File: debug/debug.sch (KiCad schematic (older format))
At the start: 6 parts

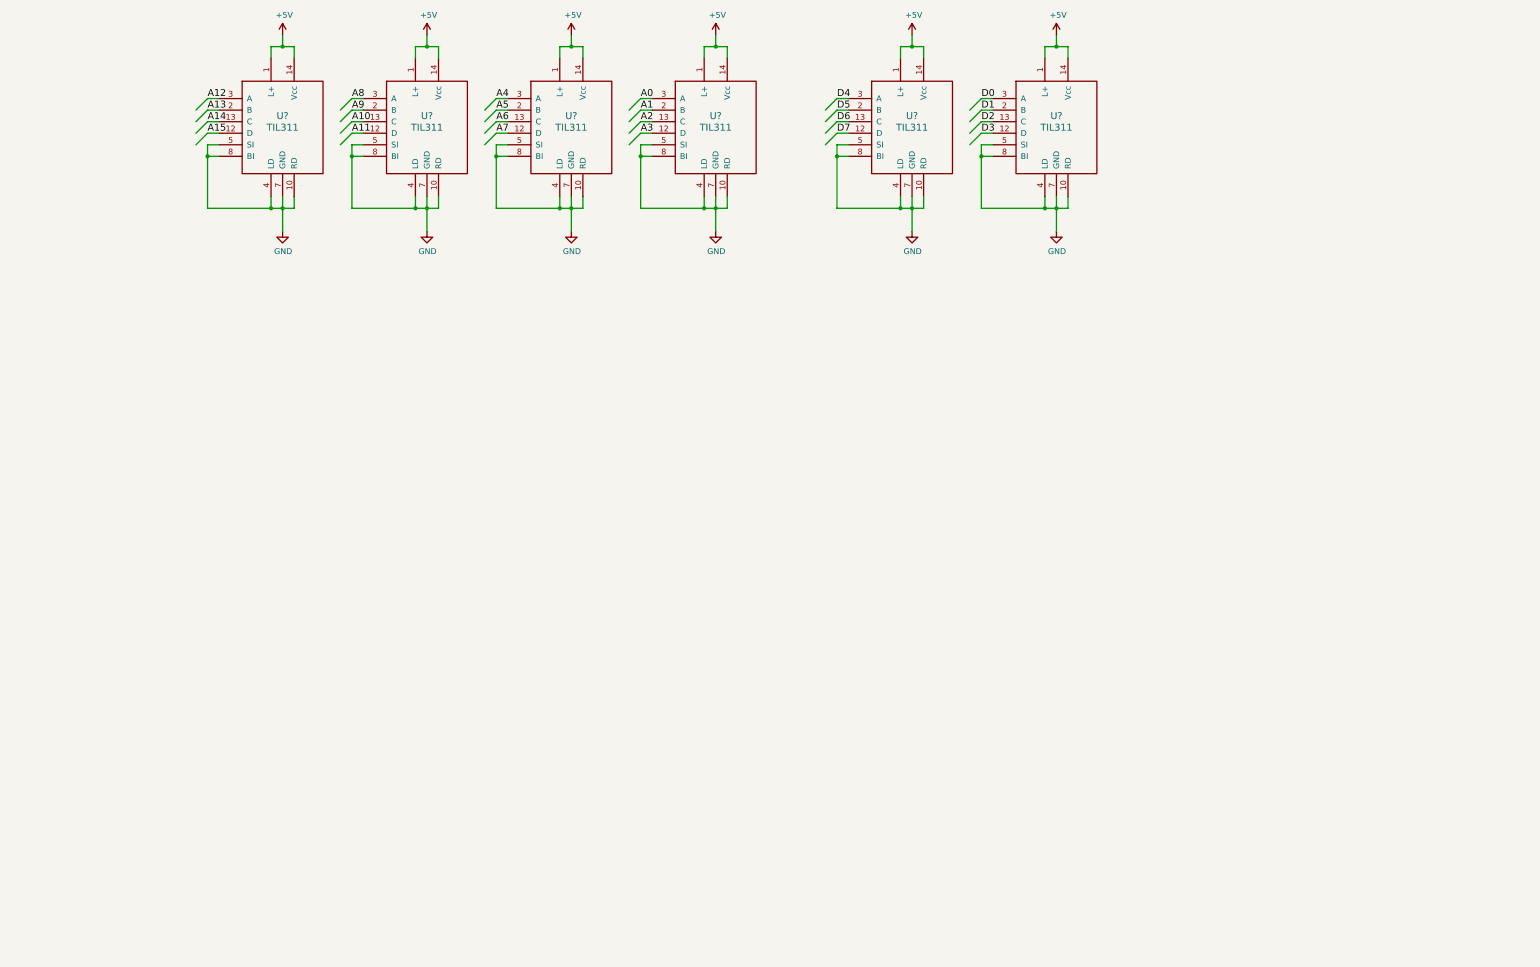
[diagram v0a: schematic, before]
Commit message: Display layout on debug board
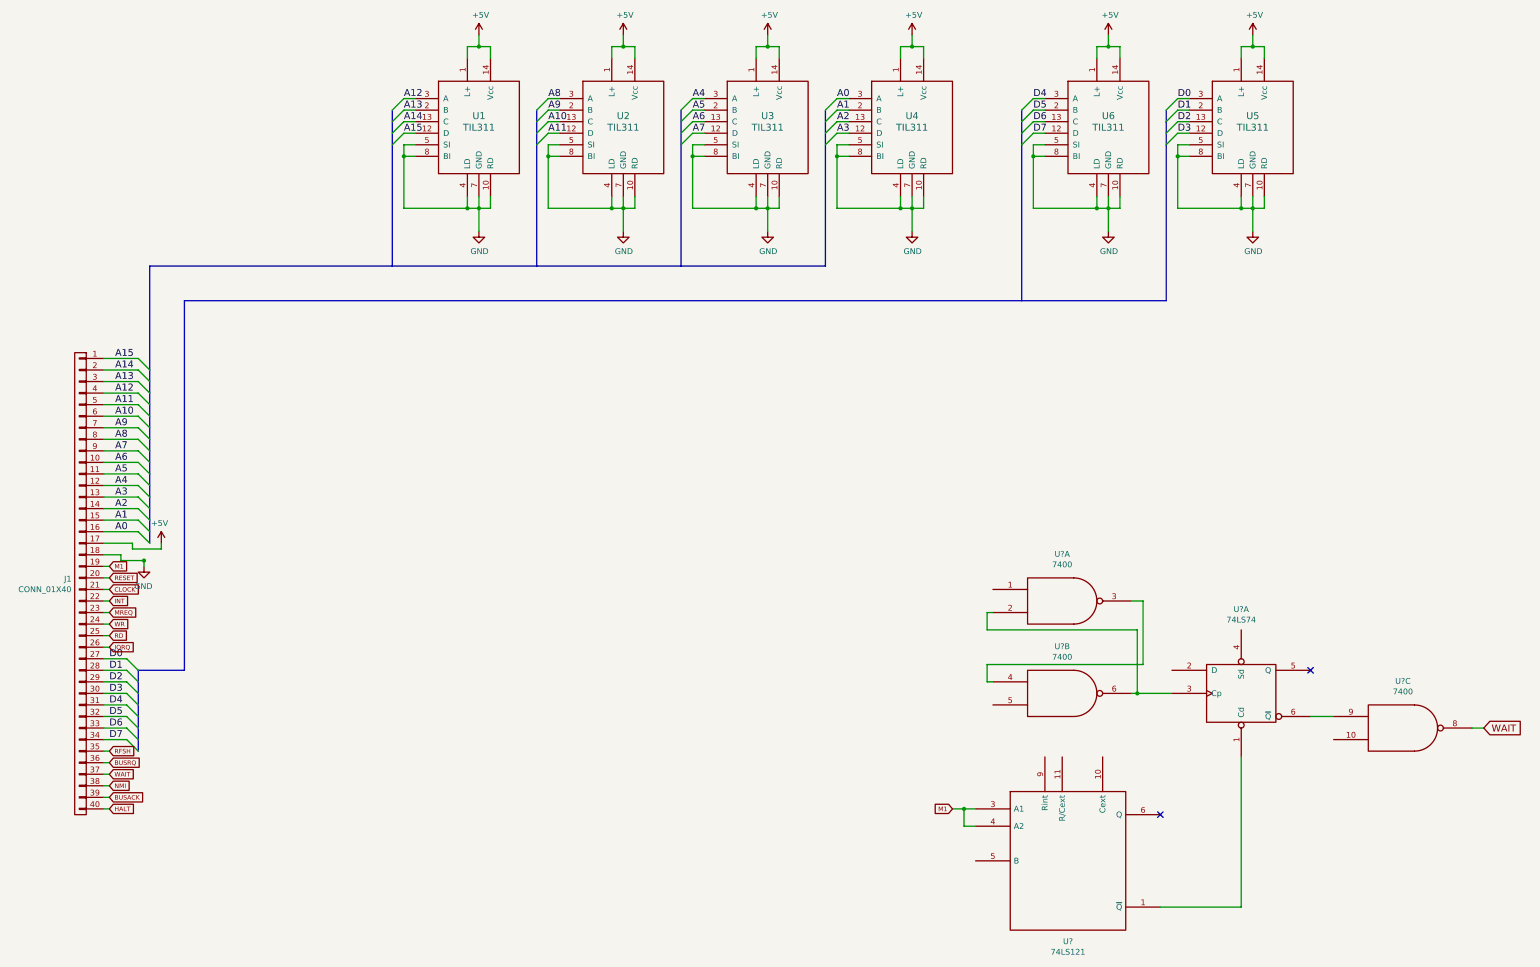
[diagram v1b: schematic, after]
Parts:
- added J1: CONN_01X40, Pin_Headers:Pin_Header_Straight_2x20_Pitch2.54mm, symbol CONN_01X40
- added U?: 74LS121, symbol 74LS121
- added U?: 74LS74, symbol 74LS74
- added U? (x3): 7400, symbol 7400
- U1, U2, U3, U4, U5, U6: renamed from U?; footprint (none) -> z80:DIP-14_W7.62mm_Socket
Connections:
- net +5V: now also J1.17 (P17)
- net A0: now also J1.16 (P16)
- net A1: now also J1.15 (P15)
- net A10: now also J1.6 (P6)
- net A11: now also J1.5 (P5)
- net A12: now also J1.4 (P4)
- net A13: now also J1.3 (P3)
- net A14: now also J1.2 (P2)
- net A15: now also J1.1 (P1)
- net A2: now also J1.14 (P14)
- net A3: now also J1.13 (P13)
- net A4: now also J1.12 (P12)
- net A5: now also J1.11 (P11)
- net A6: now also J1.10 (P10)
- net A7: now also J1.9 (P9)
- net A8: now also J1.8 (P8)
- net A9: now also J1.7 (P7)
- net D0: now also J1.27 (P27)
- net D1: now also J1.28 (P28)
- net D2: now also J1.29 (P29)
- net D3: now also J1.30 (P30)
- net D4: now also J1.31 (P31)
- net D5: now also J1.32 (P32)
- net D6: now also J1.33 (P33)
- net D7: now also J1.34 (P34)
- net GND: now also J1.18 (P18), U?.7 (GND), U?.7 (GND), U?.7 (GND), U?.7 (GND), U?.7 (GND)
- new net: U?.1 (Cd), U?.1 (~Q)
- new net: U?.2, U?.3 (Cp), U?.6
- new net: U?.6 (~Q), U?.9
- new net: U?.3, U?.4
- new net BUSACK: J1.39 (P39)
- new net BUSRQ: J1.36 (P36)
- new net CLOCK: J1.21 (P21)
- new net HALT: J1.40 (P40)
- new net INT: J1.22 (P22)
- new net IORQ: J1.26 (P26)
- new net M1: J1.19 (P19), U?.3 (A1), U?.4 (A2)
- new net MREQ: J1.23 (P23)
- new net NMI: J1.38 (P38)
- new net RD: J1.25 (P25)
- new net RESET: J1.20 (P20)
- new net RFSH: J1.35 (P35)
- new net VCC: U?.14 (VCC), U?.14 (VCC), U?.14 (VCC), U?.14 (VCC), U?.14 (VCC)
- new net WAIT: J1.37 (P37), U?.8
- new net WR: J1.24 (P24)
- no-connect marks 0 -> 2
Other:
- moved on the sheet: U1, U2, U3, U4, U5, U6
